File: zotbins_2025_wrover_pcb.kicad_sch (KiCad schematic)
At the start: 41 parts, among them J1 FFC2B28-24-G, J10 DCJ200-10-A-XX-K_REVA, J2 DCJ200-10-A-XX-K_REVA, J3 HC-SR04_Screw_Terminal_01x04, J4 HX711_Screw_Terminal_01x04, J5 Main_Servo_Screw_Terminal_01x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, J6 Conn_01x30_Pin, J7 SG_Servo_Screw_Terminal_01x03, J8 BB_Receiver_Screw_Terminal_01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, J9 BB_Transmitter_Screw_Terminal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

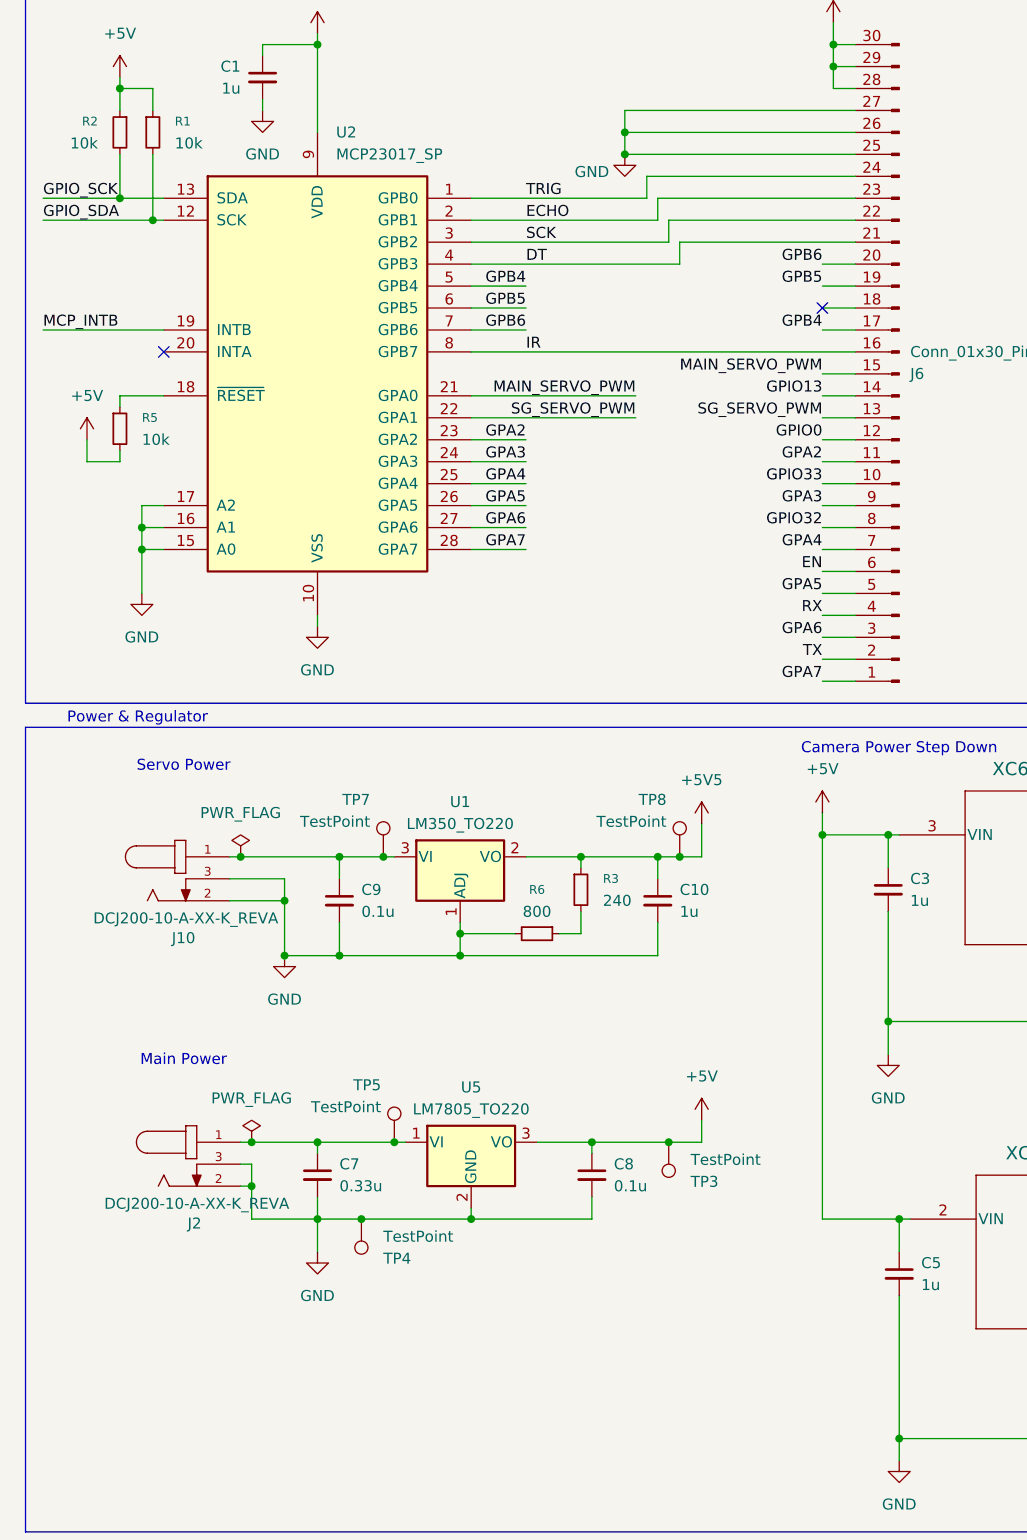
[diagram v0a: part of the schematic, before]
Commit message: SCHEMATIC EDITS ONLY: remodified servo power to be unified under 1 barrel jack. Interrupt pins rerouted.
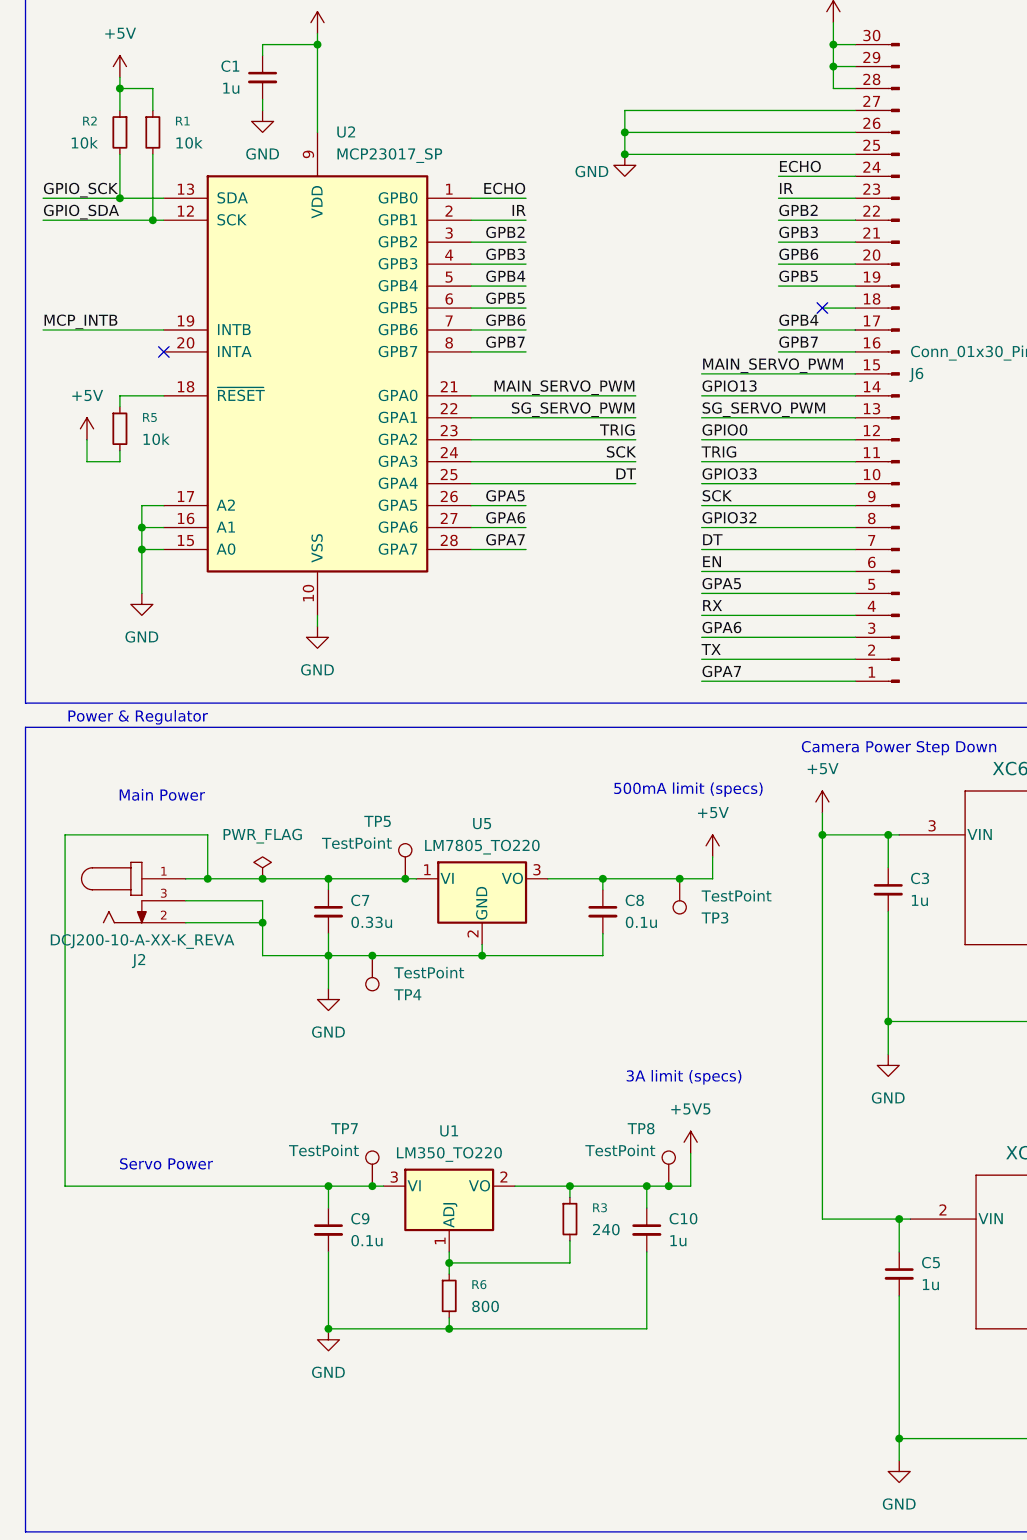
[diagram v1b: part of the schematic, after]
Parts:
- removed J10: DCJ200-10-A-XX-K_REVA, Library:GCT_DCJ200-10-A-XX-K_REVA, symbol DCJ200-10-A-XX-K_REVA:DCJ200-10-A-XX-K_REVA
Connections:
- net GPA2 is gone; now on net TRIG: J6.11 (Pin_11), U2.23 (GPA2)
- net GPA3 is gone; now on net SCK: J6.9 (Pin_9), U2.24 (GPA3)
- net GPA4 is gone; now on net DT: J6.7 (Pin_7), U2.25 (GPA4)
- net DT: no longer J6.21 (Pin_21), U2.4 (GPB3)
- net ECHO: now also J6.24 (Pin_24), U2.1 (GPB0); no longer J6.23 (Pin_23), U2.2 (GPB1)
- net GND: no longer U1.1 (ADJ)
- net IR: now also J6.23 (Pin_23), U2.2 (GPB1); no longer J6.16 (Pin_16), U2.8 (GPB7)
- net SCK: no longer J6.22 (Pin_22), U2.3 (GPB2)
- net TRIG: no longer J6.24 (Pin_24), U2.1 (GPB0)
- net at C7.1, J2.1, TP5.1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: now also C9.1, TP7.1, U1.3 (VI)
- net at R3.2, R6.1: now also U1.1 (ADJ)
- new net GPB2: J6.22 (Pin_22), U2.3 (GPB2)
- new net GPB3: J6.21 (Pin_21), U2.4 (GPB3)
- new net GPB7: J6.16 (Pin_16), U2.8 (GPB7)
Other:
- note added: "3A limit (specs)"
- note added: "500mA limit (specs)"
- moved on the sheet: C10, C7, C8, C9, J2, R3, R6, TP3, TP4, TP5, TP7, TP8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

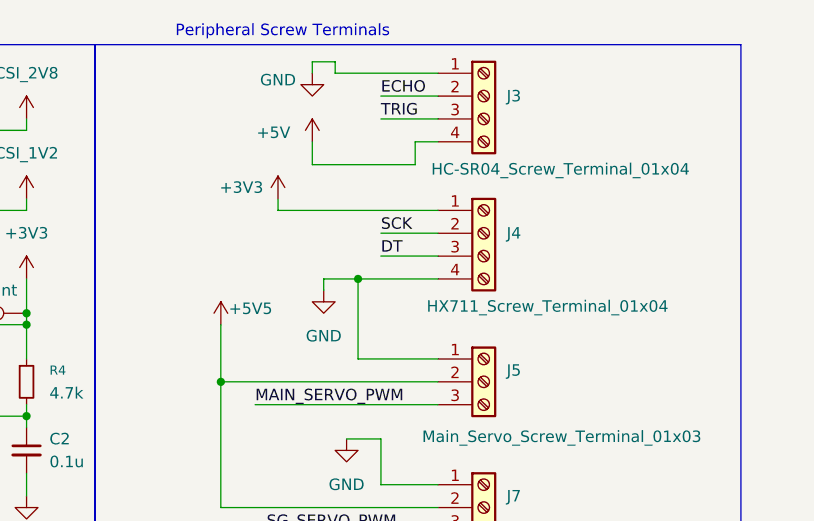
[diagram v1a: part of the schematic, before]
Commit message: hx711 bug update -- Digikey vendor sells different version of hx711 -> updated schematic + footprint
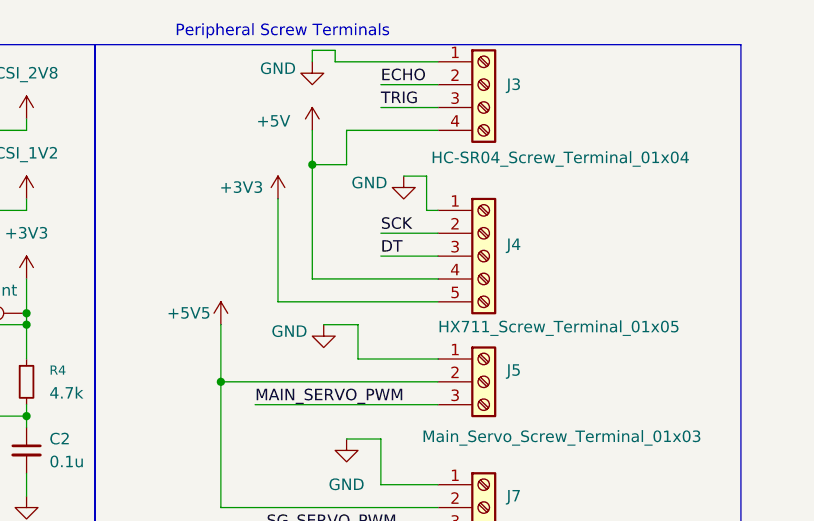
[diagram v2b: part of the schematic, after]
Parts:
- removed J4: HX711_Screw_Terminal_01x04, TerminalBlock_4Ucon:TerminalBlock_4Ucon_1x04_P3.50mm_Vertical, symbol Connector:Screw_Terminal_01x04
- added J4: HX711_Screw_Terminal_01x05, TerminalBlock_4Ucon:TerminalBlock_4Ucon_1x05_P3.50mm_Vertical, symbol Connector:Screw_Terminal_01x05
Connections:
- net +3V3: now also J4.5 (Pin_5)
- net +5V: now also J4.4 (Pin_4)
- net DT: now also J4.3 (Pin_3)
- net GND: now also J4.1 (Pin_1)
- net SCK: now also J4.2 (Pin_2)
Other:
- moved on the sheet: J3

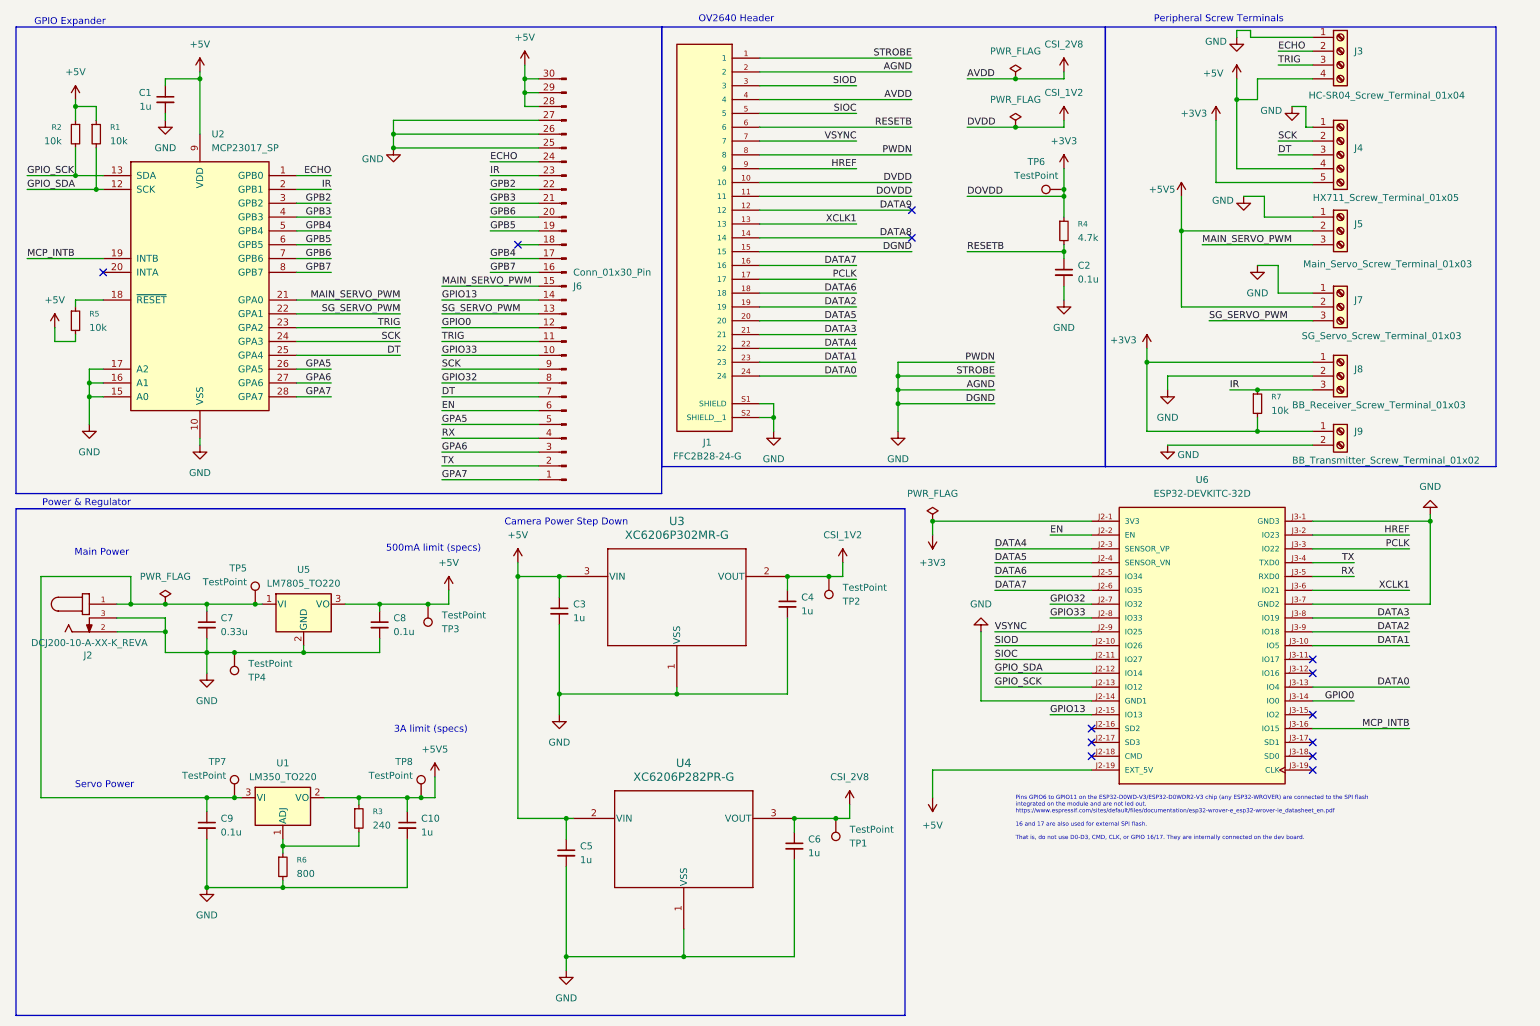
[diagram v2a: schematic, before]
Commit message: Schematic work only: added LED circuitry, bug fixes on GPIO expander (5V -> 3.3V).
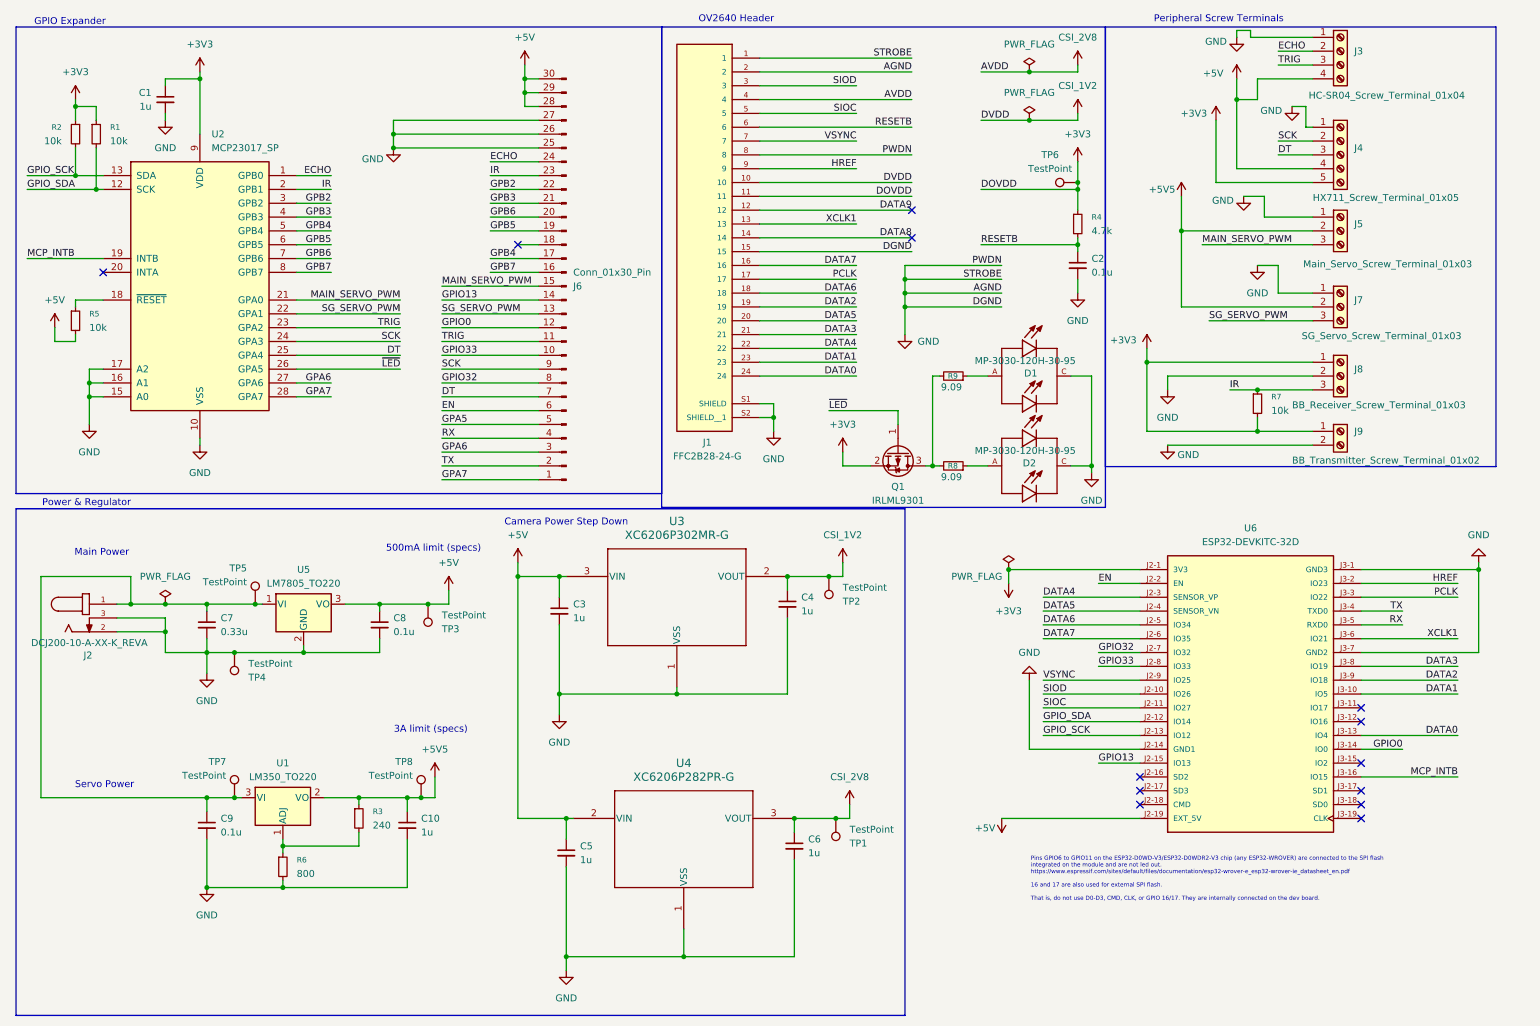
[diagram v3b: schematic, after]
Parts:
- added D1, D2: MP-3030-120H-30-95, LED:LED_MP-3030-120H-30-95, symbol LED-Flash:MP-3030-120H-30-95
- added Q1: IRLML9301, Package_TO_SOT_SMD:SOT-23, symbol Transistor_FET:IRLML9301
- added R8, R9: 9.09, Resistor_THT:R_Axial_DIN0207_L6.3mm_D2.5mm_P10.16mm_Horizontal, symbol Device:R_Small
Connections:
- net +3V3: now also C1.1, R1.1, R2.1, U2.9 (VDD), Q1.2 (S)
- net +5V: no longer C1.1, R1.1, R2.1, U2.9 (VDD)
- net GND: now also D1.C, D2.C
- net GPA5: no longer U2.26 (GPA5)
- new net: D2.A, R8.1
- new net: Q1.3 (D), R8.2, R9.2
- new net: D1.A, R9.1
- new net ~{LED}: Q1.1 (G), U2.26 (GPA5)
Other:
- moved on the sheet: C2, R4, TP6, U6

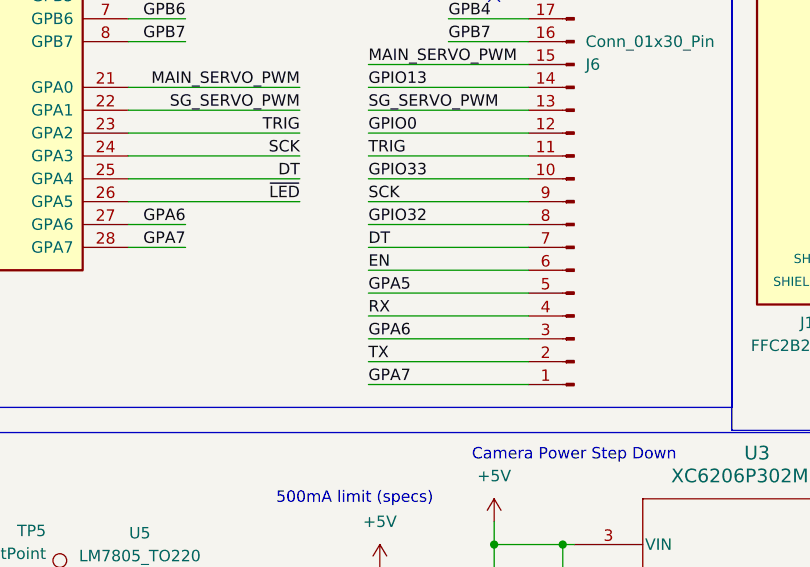
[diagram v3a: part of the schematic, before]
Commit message: completed PCB changes for iteration 2
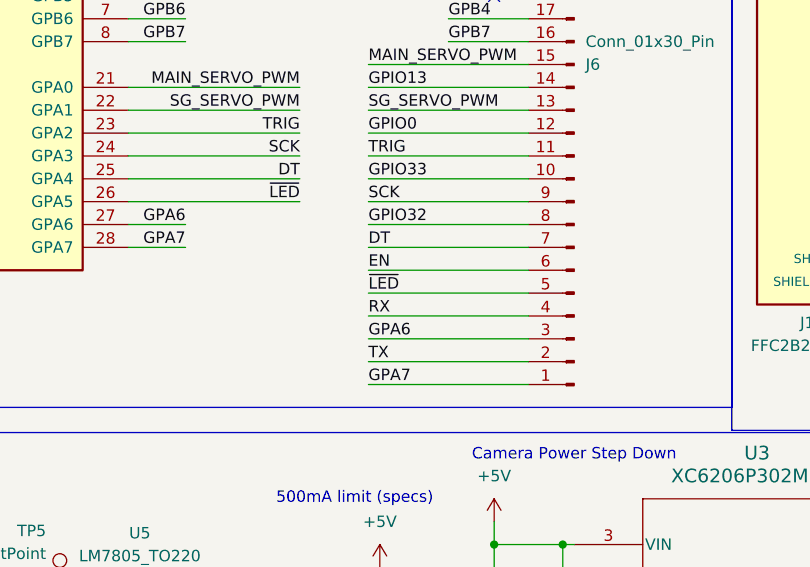
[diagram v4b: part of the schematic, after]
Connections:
- net GPA5 is gone; now on net ~{LED}: J6.5 (Pin_5)
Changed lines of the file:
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@@
+		)
+	)
+	(label "~{LED}"
+		(at 90.17 88.9 0)
+		(effects
+			(font
+				(size 1.27 1.27)
+			)
+			(justify left bottom)
 		)
 	)
@@
 		)
 	)
-	(label "GPA5"
-		(at 90.17 88.9 0)
-		(effects
-			(font
-				(size 1.27 1.27)
-			)
-			(justify left bottom)
-		)
-	)
